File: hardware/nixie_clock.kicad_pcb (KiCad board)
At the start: 2 copper layers, 224 x 70 mm, 79 parts, among them J1 Conn_02x02_Odd_Even, J2 USB_C_Receptacle_USB2.0_16P, J7 Barrel_Jack_Switch, Q1 IRF740, U1 AP63203WU, U2 MAX1771xSA, U3 ESP32-C3-WROOM-02, U4 HV5622PG, U5 HV5622PG

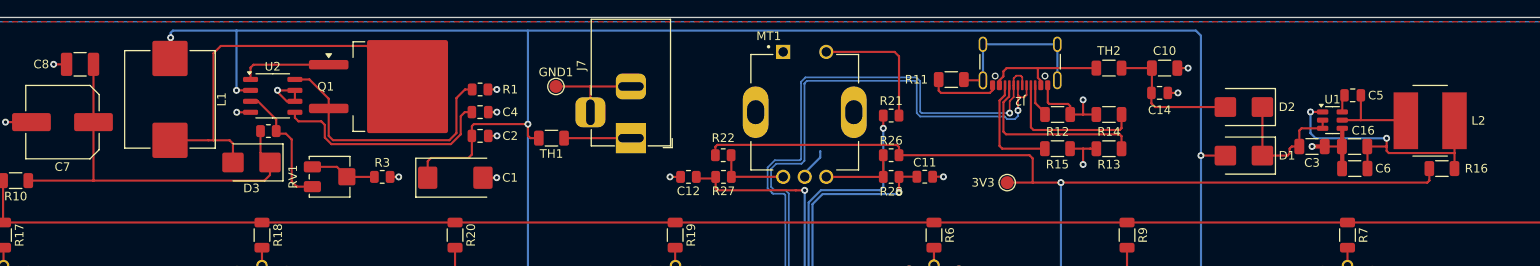
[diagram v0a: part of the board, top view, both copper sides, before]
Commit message: Add capacitor for rotary switch.
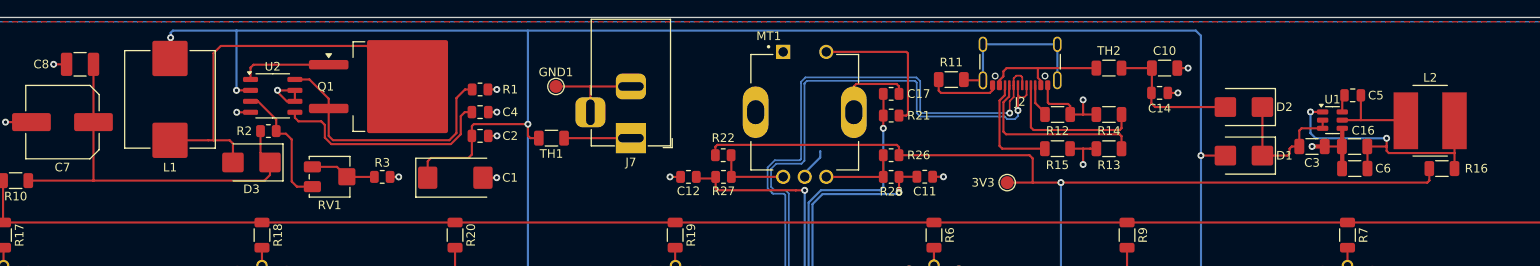
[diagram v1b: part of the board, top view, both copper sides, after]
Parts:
- added C17: 100nF, Resistor_SMD:R_0805_2012Metric, F.Cu at (172.0, 68.9)
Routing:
- net /connectors/GND: track 112.3 -> 121.6 mm
- net Net-(U3-IO3): track 62.9 -> 65.5 mm
- net Net-(MT1-Pad2): track 15.5 -> 17.7 mm

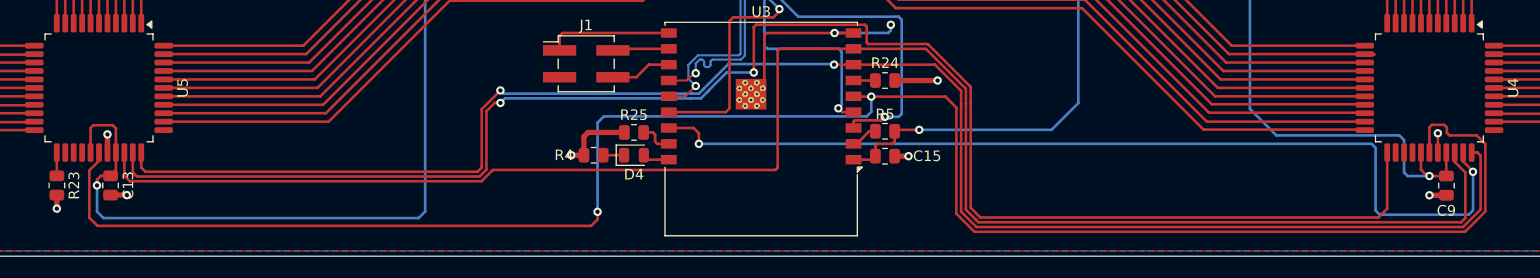
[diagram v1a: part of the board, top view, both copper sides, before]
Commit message: Add IO1 to pin header. Add .step models.
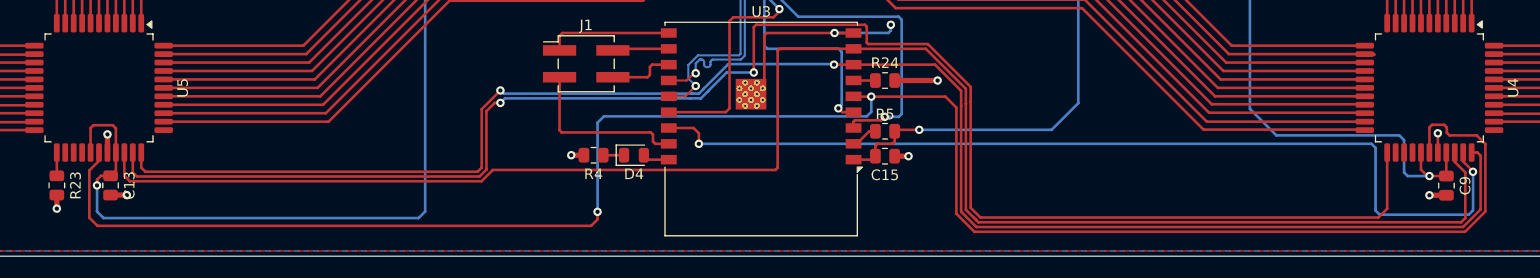
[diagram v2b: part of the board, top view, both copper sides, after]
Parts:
- removed R25: 10k, Resistor_SMD:R_0805_2012Metric
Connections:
- J1 pad 3: /connectors/GND -> Net-(J1-Pin_3)
- U3 pad 17: Net-(U3-IO1) -> Net-(J1-Pin_3)
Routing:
- net Net-(J1-Pin_3): track 0.00 -> 16.3 mm
- net /connectors/GND: track 121.6 -> 115.8 mm
- net Net-(U3-IO1): track 3.22 -> 0.00 mm

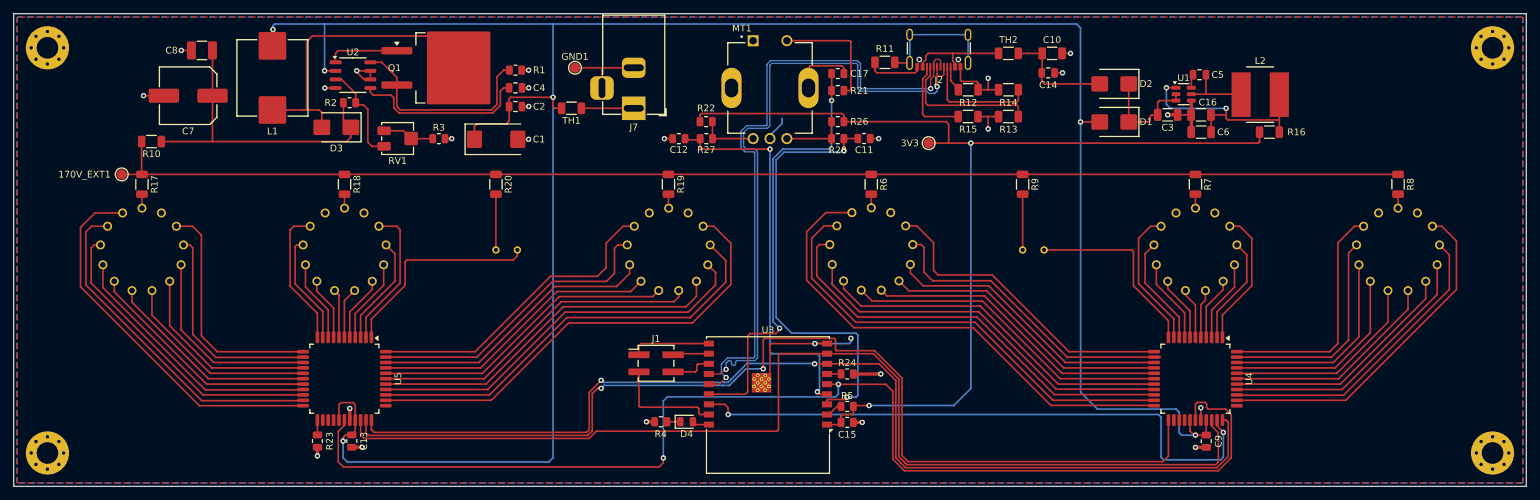
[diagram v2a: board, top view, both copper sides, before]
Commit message: Add via stitching.
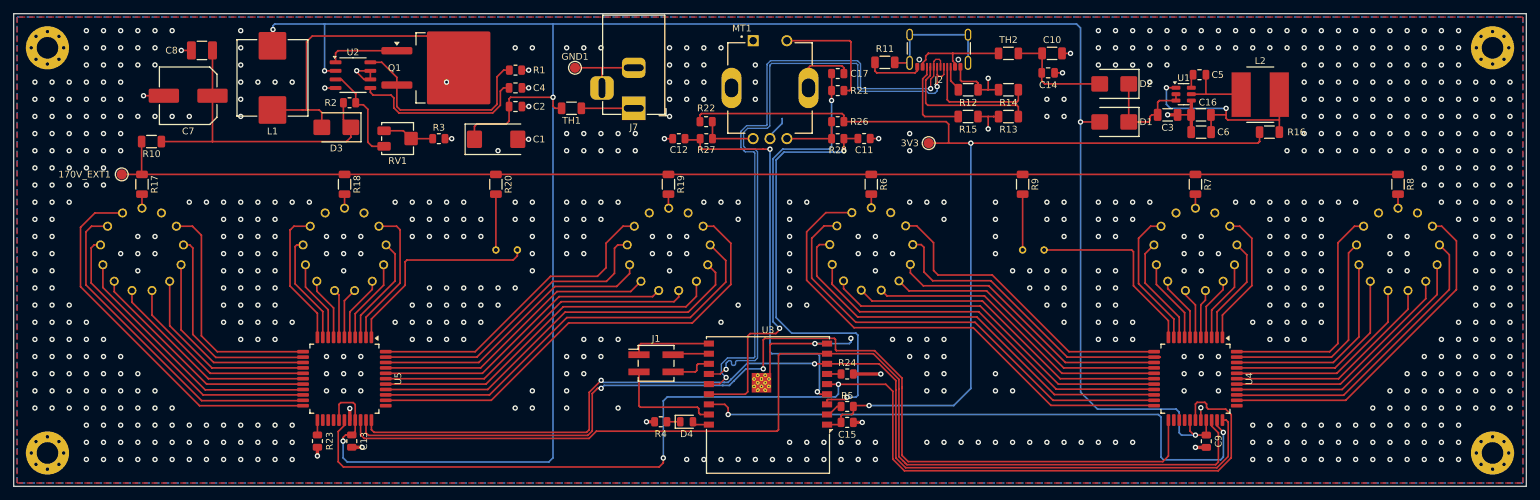
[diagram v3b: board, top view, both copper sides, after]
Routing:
- net /connectors/GND: vias 26 -> 778

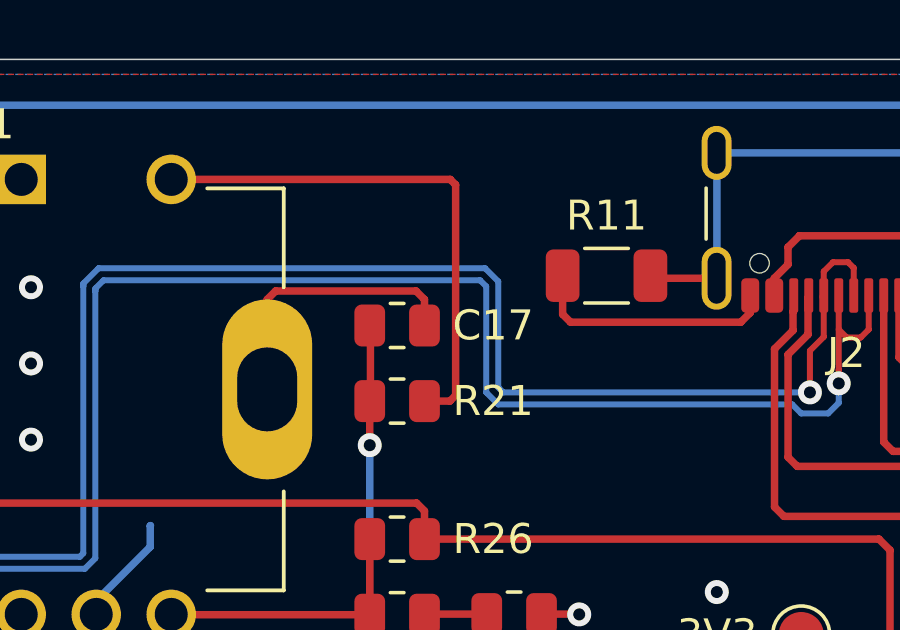
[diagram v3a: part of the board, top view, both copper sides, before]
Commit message: Remove useless 10k resistor for PEC11 switch.
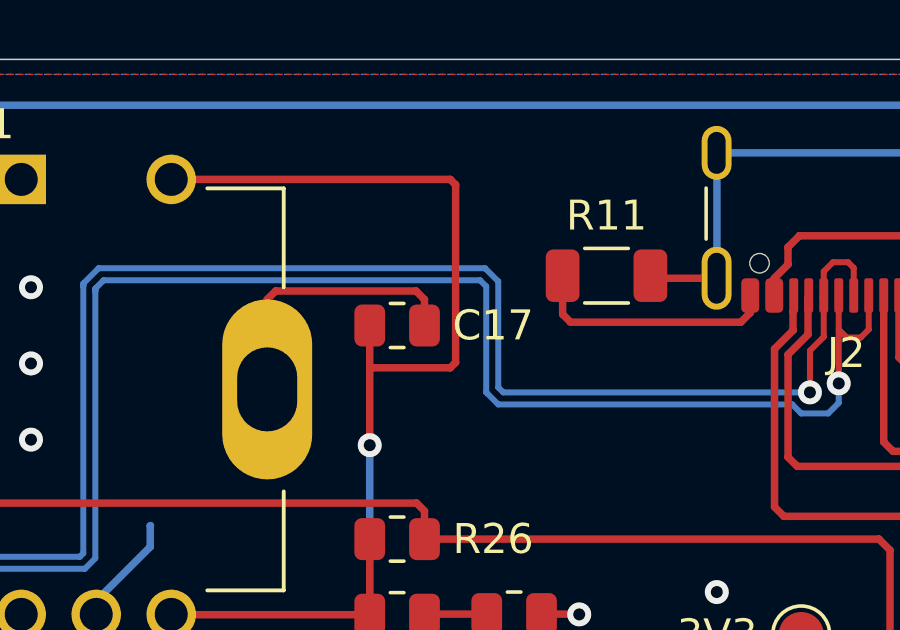
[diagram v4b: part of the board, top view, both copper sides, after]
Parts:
- removed R21: 10k, Resistor_SMD:R_0805_2012Metric
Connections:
- MT1 pad 2: Net-(MT1-Pad2) -> Net-(U3-IO3)
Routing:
- net Net-(U3-IO3): track 65.5 -> 83.8 mm
- net Net-(MT1-Pad2): track 17.7 -> 0.00 mm

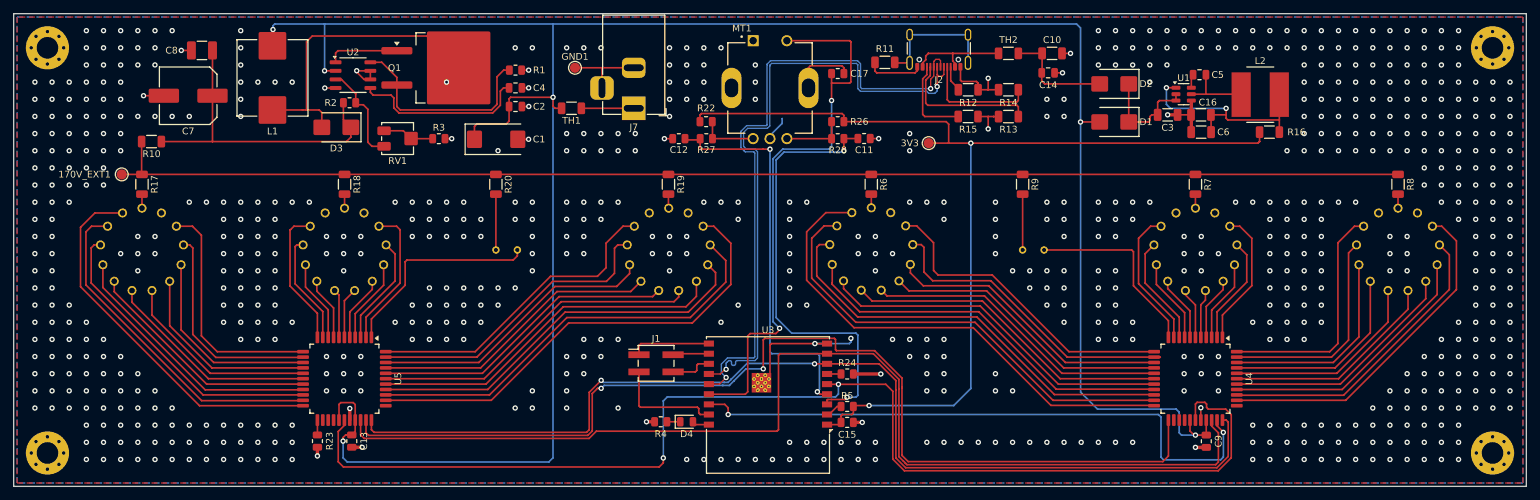
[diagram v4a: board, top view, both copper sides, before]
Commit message: Add BOOT1 and RESET1 buttons. Add pullups on Boot strapping pins GPIO8,9. Fix EN, enable input.
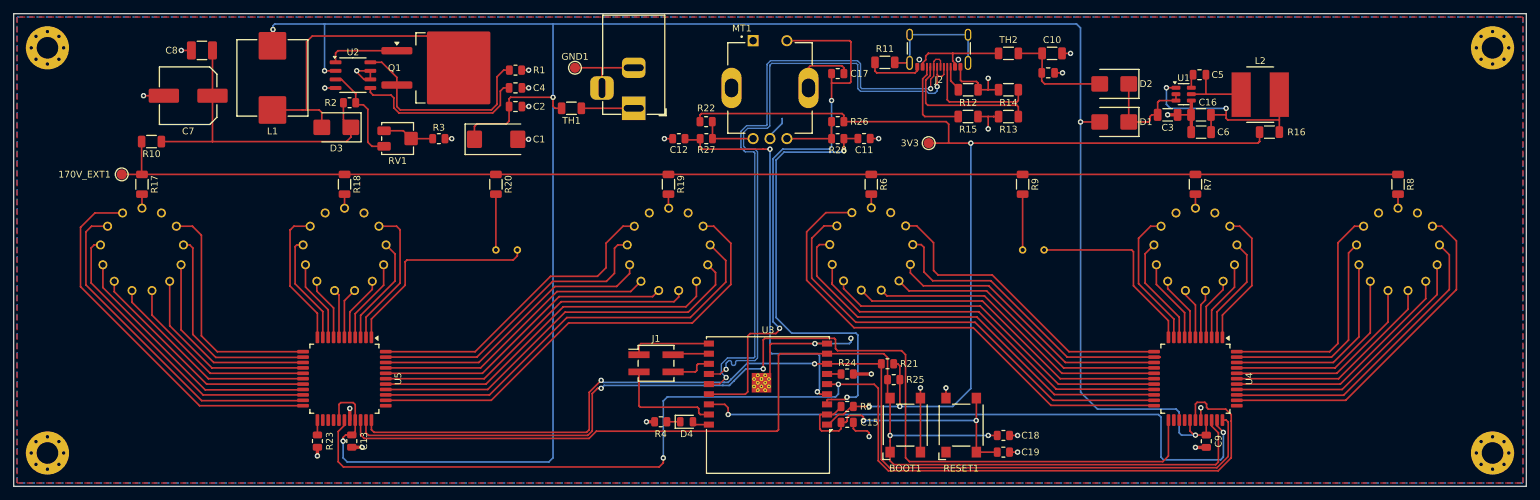
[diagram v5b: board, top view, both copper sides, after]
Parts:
- added BOOT1: SW_Push, Button_Switch_SMD:SW_SPST_Omron_B3FS-100xP, F.Cu at (182.0, 120.9)
- added C18: 100nF, Resistor_SMD:R_0805_2012Metric, F.Cu at (196.6, 122.5)
- added C19: 100nf, Resistor_SMD:R_0805_2012Metric, F.Cu at (196.6, 124.9)
- added R21: 10k, Resistor_SMD:R_0805_2012Metric, F.Cu at (179.4, 111.8)
- added R25: 10k, Resistor_SMD:R_0805_2012Metric, F.Cu at (180.3, 114.2)
- added RESET1: SW_Push, Button_Switch_SMD:SW_SPST_Omron_B3FS-100xP, F.Cu at (190.3, 120.9)
- C15: value 100nF -> 1uF
- turned C15 to 180 degrees
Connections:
- C15 pad 1: /cpu/3.3V -> /connectors/GND
- C15 pad 2: /connectors/GND -> Net-(U3-EN)
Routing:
- net Net-(U3-EN): track 2.56 -> 42.7 mm, vias 0 -> 2
- net /cpu/GPIO2: track 162.3 -> 180.0 mm, vias 0 -> 2
- net /connectors/GND: track 115.8 -> 131.0 mm, vias 778 -> 30
- net /cpu/3.3V: track 152.6 -> 159.3 mm, vias 2 -> 3
- net /driver_3_digits_1_dot_left/SPI_SDO: track 153.4 -> 155.5 mm
- net /cpu/GPIO1: track 156.0 -> 157.6 mm

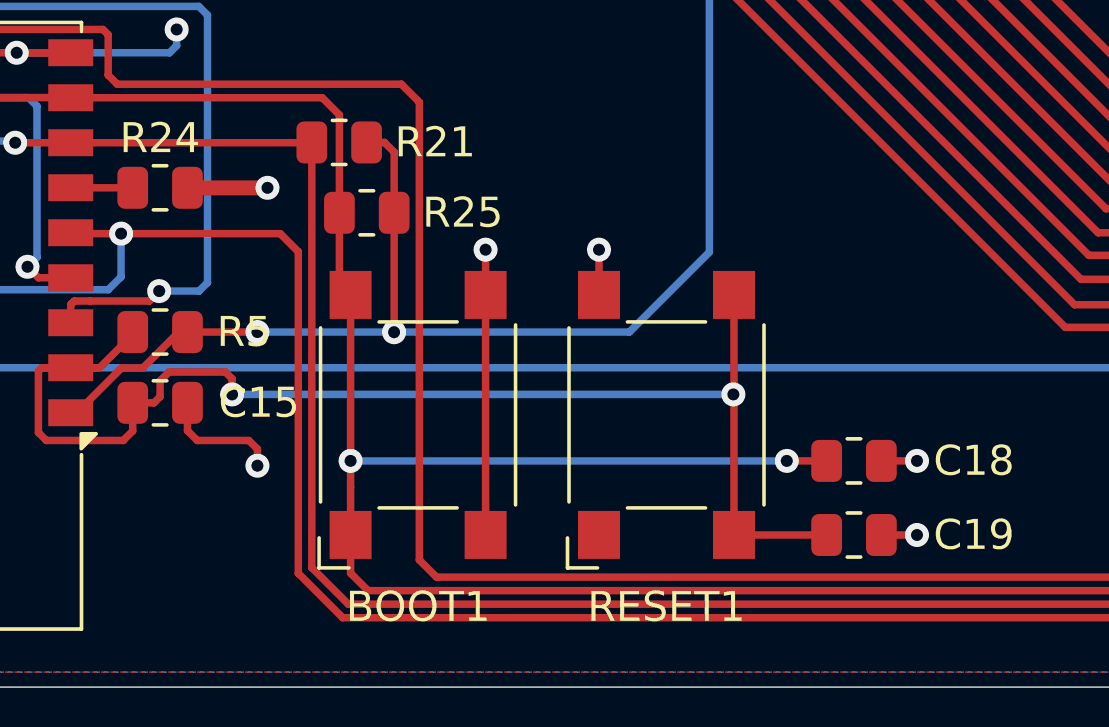
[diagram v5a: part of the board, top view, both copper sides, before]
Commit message: Removed useless vias.
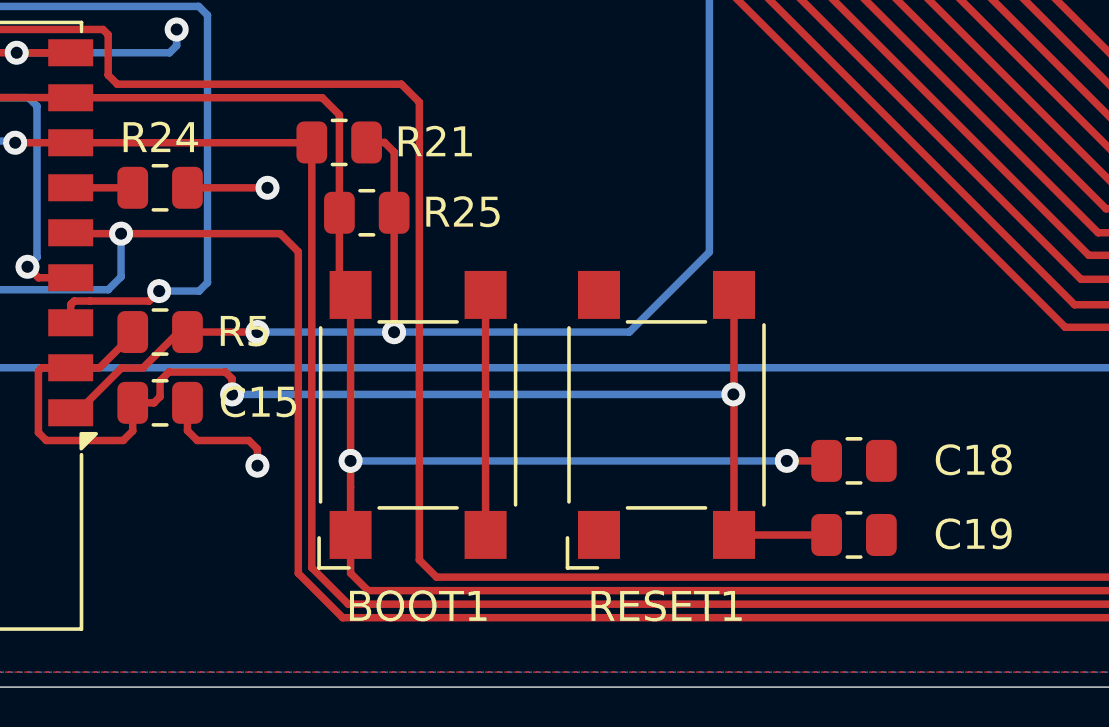
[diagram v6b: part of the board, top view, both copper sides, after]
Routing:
- net /connectors/GND: track 131.0 -> 125.6 mm, vias 30 -> 26
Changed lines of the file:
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@@
-	)
-	(segment
-		(start 188.06 116.9275)
-		(end 188.06 115.54)
-		(width 0.25)
-		(layer "F.Cu")
-		(net 123)
 	)
 	(segment
@@
 	)
 	(segment
-		(start 197.4725 124.93)
-		(end 198.66 124.93)
-		(width 0.25)
-		(layer "F.Cu")
-		(net 123)
-	)
-	(segment
 		(start 167.98 67.72)
 		(end 167.7 68)
@@
 		(start 177.01 113.358)
 		(end 174.3435 113.358)
-		(width 0.5)
+		(width 0.25)
 		(layer "F.Cu")
 		(net 123)
@@
 	)
 	(segment
-		(start 174.755752 113.346748)
-		(end 174.7455 113.357)
-		(width 0.5)
-		(layer "F.Cu")
-		(net 123)
-	)
-	(segment
-		(start 197.4725 122.46)
-		(end 198.76 122.46)
-		(width 0.25)
-		(layer "F.Cu")
-		(net 123)
-	)
-	(segment
 		(start 190.209992 68.46)
 		(end 190.209992 69.865)
@@
 	)
 	(segment
-		(start 184.28 116.9275)
-		(end 184.28 115.42)
-		(width 0.25)
-		(layer "F.Cu")
-		(net 123)
-	)
-	(segment
 		(start 141.819792 68.01)
 		(end 141.819792 68.26)
@@
 	)
 	(via
-		(at 198.66 122.46)
-		(size 0.8)
-		(drill 0.4)
-		(layers "F.Cu" "B.Cu")
-		(net 123)
-	)
-	(via
 		(at 177.01 113.358)
 		(size 0.8)
@@
 	)
 	(via
-		(at 184.28 115.42)
-		(size 0.8)
-		(drill 0.4)
-		(layers "F.Cu" "B.Cu")
-		(net 123)
-	)
-	(via
 		(at 178.1 78.5)
 		(size 0.8)
@@
 	)
 	(via
-		(at 198.66 124.93)
-		(size 0.8)
-		(drill 0.4)
-		(layers "F.Cu" "B.Cu")
-		(net 123)
-	)
-	(via
 		(at 96.072292 71.0075)
 		(size 0.8)
@@
 		(size 0.8)
 		(drill 0.4)
-		(layers "F.Cu" "B.Cu")
-		(net 123)
-	)
-	(via
-		(at 188.06 115.42)
-		(size 0.8)
-		(drill 0.4)
